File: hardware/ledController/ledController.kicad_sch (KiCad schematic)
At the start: 23 parts, among them IC1 PIC16F1769-I_ML, J1 Conn_01x06, J2 Screw_Terminal_01x02, J3 Screw_Terminal_01x02, J4 Conn_01x06, J5 Conn_01x02_Male

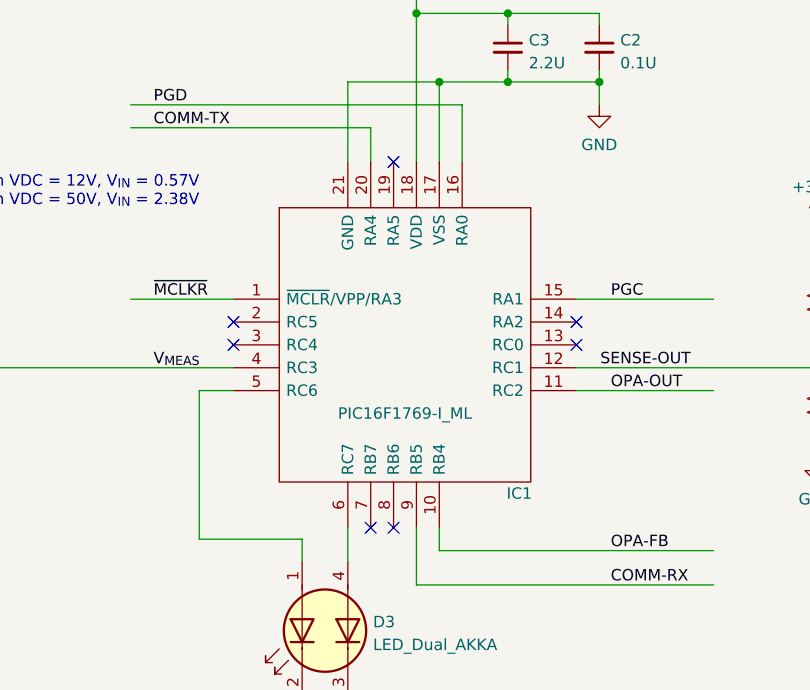
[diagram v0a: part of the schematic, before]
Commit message: Version V1.1
Replaced PIC16F1769 with PIC16LF1709.  They are pin-to-pin
compatible with each other
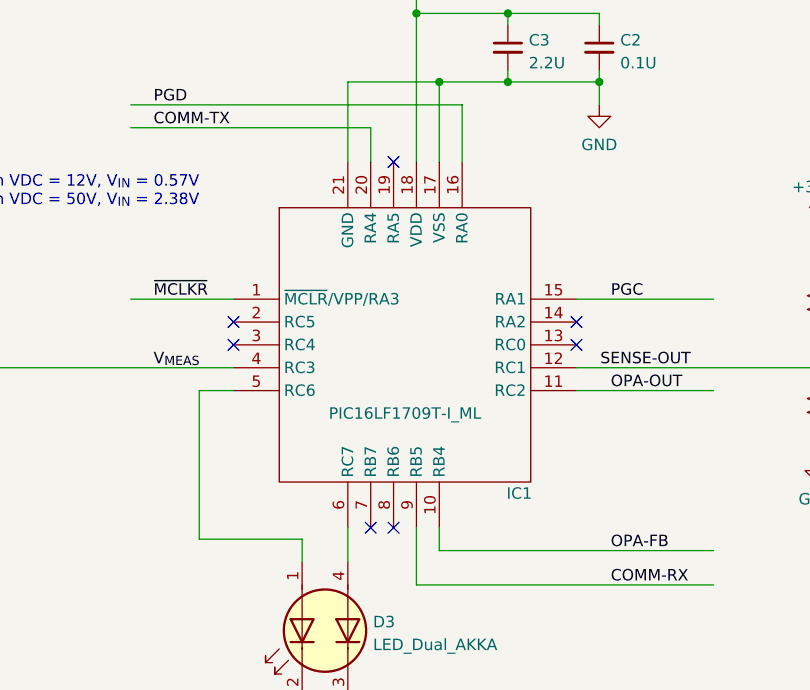
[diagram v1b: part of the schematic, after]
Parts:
- removed IC1: PIC16F1769-I_ML, footprints:QFN50P400X400X100-21N-D, symbol PIC16F1769-I_ML:PIC16F1769-I_ML
- added IC1: PIC16LF1709T-I_ML, Package_DFN_QFN:QFN-20-1EP_4x4mm_P0.5mm_EP2.5x2.5mm, symbol ym_Microcontrollers:PIC16LF1709T-I_ML
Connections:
- net +3.3V: now also IC1.18 (VDD)
- net COMM-RX: now also IC1.9 (RB5)
- net COMM-TX: now also IC1.20 (RA4)
- net GND: now also IC1.17 (VSS), IC1.21 (GND)
- net OPA-FB: now also IC1.10 (RB4)
- net OPA-OUT: now also IC1.11 (RC2)
- net PGC: now also IC1.15 (RA1)
- net PGD: now also IC1.16 (RA0)
- net SENSE-OUT: now also IC1.12 (RC1)
- net V_{MEAS}: now also IC1.4 (RC3)
- net ~{MCLKR}: now also IC1.1 (~{MCLR}/VPP/RA3)
- net at D3.1 (A1): now also IC1.5 (RC6)
- net at D3.4 (A2): now also IC1.6 (RC7)
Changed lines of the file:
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@@
   (title_block
     (title "Lantern")
+    (date "2023-01-09")
+    (rev "V1.1")
   )
   (junction (at 210.82 64.77) (diameter 0) (color 0 0 0 0)
@@
     (pin "2")
   )
-  (symbol (lib_id "PIC16F1769-I_ML:PIC16F1769-I_ML") (at 180.34 88.9 0) (unit 1)
+  (symbol (lib_id "Device:C_Small") (at 220.98 60.96 0) (unit 1)
+    (in_bom yes) (on_board yes) (fields_autoplaced)
+    (property "Reference" "C2" (id 0) (at 223.3041 60.1316 0)
+      (effects (font (size 1.27 1.27)) (justify left))
+    )
+    (property "Value" "0.1U" (id 1) (at 223.3041 62.6685 0)
+      (effects (font (size 1.27 1.27)) (justify left))
+    )
+    (property "Footprint" "Capacitor_SMD:C_0402_1005Metric_Pad0.74x0.62mm_HandSolder" (id 2) (at 220.98 60.96 0)
+      (effects (font (size 1.27 1.27)) hide)
+    )
+    (property "Datasheet" "~" (id 3) (at 220.98 60.96 0)
+      (effects (font (size 1.27 1.27)) hide)
+    )
+    (pin "1")
+    (pin "2")
+  )
+  (symbol (lib_id "Mechanical:MountingHole") (at 172.72 17.78 0) (unit 1)
+    (in_bom yes) (on_board yes) (fields_autoplaced)
+    (property "Reference" "H1" (id 0) (at 175.26 16.9453 0)
+      (effects (font (size 1.27 1.27)) (justify left))
+    )
+    (property "Value" "MountingHole" (id 1) (at 175.26 19.4822 0)
+      (effects (font (size 1.27 1.27)) (justify left))
+    )
+    (property "Footprint" "MountingHole:MountingHole_2.5mm_Pad_TopBottom" (id 2) (at 172.72 17.78 0)
+      (effects (font (size 1.27 1.27)) hide)
+    )
+    (property "Datasheet" "~" (id 3) (at 172.72 17.78 0)
+      (effects (font (size 1.27 1.27)) hide)
+    )
+  )
+  (symbol (lib_id "Device:C_Small") (at 210.82 60.96 0) (unit 1)
+    (in_bom yes) (on_board yes) (fields_autoplaced)
+    (property "Reference" "C3" (id 0) (at 213.1441 60.1316 0)
+      (effects (font (size 1.27 1.27)) (justify left))
+    )
+    (property "Value" "2.2U" (id 1) (at 213.1441 62.6685 0)
+      (effects (font (size 1.27 1.27)) (justify left))
+    )
+    (property "Footprint" "Capacitor_SMD:C_0402_1005Metric_Pad0.74x0.62mm_HandSolder" (id 2) (at 210.82 60.96 0)
+      (effects (font (size 1.27 1.27)) hide)
+    )
+    (property "Datasheet" "~" (id 3) (at 210.82 60.96 0)
+      (effects (font (size 1.27 1.27)) hide)
+    )
+    (pin "1")
+    (pin "2")
+  )
+  (symbol (lib_id "Device:R_Small_US") (at 187.96 140.97 0) (unit 1)
+    (in_bom yes) (on_board yes)
+    (property "Reference" "R11" (id 0) (at 181.61 139.7 0)
+      (effects (font (size 1.27 1.27)) (justify left))
+    )
+    (property "Value" "2.4K" (id 1) (at 181.61 142.24 0)
+      (effects (font (size 1.27 1.27)) (justify left))
+    )
+    (property "Footprint" "Resistor_SMD:R_0603_1608Metric_Pad0.98x0.95mm_HandSolder" (id 2) (at 187.96 140.97 0)
+      (effects (font (size 1.27 1.27)) hide)
+    )
+    (property "Datasheet" "~" (id 3) (at 187.96 140.97 0)
+      (effects (font (size 1.27 1.27)) hide)
+    )
+    (pin "1")
+    (pin "2")
+  )
+  (symbol (lib_id "ym_Microcontrollers:PIC16LF1709T-I_ML") (at 199.39 93.98 0) (unit 1)
     (in_bom yes) (on_board yes)
     (property "Reference" "IC1" (id 0) (at 212.09 110.49 0))
-    (property "Value" "PIC16F1769-I_ML" (id 1) (at 199.39 101.6 0))
-    (property "Footprint" "footprints:QFN50P400X400X100-21N-D" (id 2) (at 214.63 78.74 0)
-      (effects (font (size 1.27 1.27)) (justify left) hide)
-    )
-    (property "Datasheet" "https://componentsearchengine.com/Datasheets/1/PIC16F1769-I_ML.pdf" (id 3) (at 214.63 81.28 0)
-      (effects (font (size 1.27 1.27)) (justify left) hide)
-    )
-    (property "Description" "Microchip Technology PIC16F1769-I/ML, 8bit 8 bit CPU Microcontroller, 32MHz, 14 kB Flash, 20-Pin QFN" (id 4) (at 214.63 83.82 0)
-      (effects (font (size 1.27 1.27)) (justify left) hide)
-    )
-    (property "Height" "1" (id 5) (at 214.63 86.36 0)
-      (effects (font (size 1.27 1.27)) (justify left) hide)
-    )
-    (property "Manufacturer_Name" "Microchip" (id 6) (at 214.63 88.9 0)
-      (effects (font (size 1.27 1.27)) (justify left) hide)
-    )
-    (property "Manufacturer_Part_Number" "PIC16F1769-I/ML" (id 7) (at 214.63 91.44 0)
-      (effects (font (size 1.27 1.27)) (justify left) hide)
-    )
-    (property "Mouser Part Number" "579-PIC16F1769-I/ML" (id 8) (at 214.63 93.98 0)
-      (effects (font (size 1.27 1.27)) (justify left) hide)
-    )
-    (property "Mouser Price/Stock" "https://www.mouser.co.uk/ProductDetail/Microchip-Technology/PIC16F1769-I-ML?qs=4f%252Bx0JRcgJY9K12iAXUX4g%3D%3D" (id 9) (at 214.63 96.52 0)
-      (effects (font (size 1.27 1.27)) (justify left) hide)
-    )
-    (property "Arrow Part Number" "PIC16F1769-I/ML" (id 10) (at 214.63 99.06 0)
-      (effects (font (size 1.27 1.27)) (justify left) hide)
-    )
-    (property "Arrow Price/Stock" "https://www.arrow.com/en/products/pic16f1769-iml/microchip-technology?region=nac" (id 11) (at 214.63 101.6 0)
-      (effects (font (size 1.27 1.27)) (justify left) hide)
-    )
-    (property "Mouser Testing Part Number" "" (id 12) (at 214.63 104.14 0)
-      (effects (font (size 1.27 1.27)) (justify left) hide)
-    )
-    (property "Mouser Testing Price/Stock" "" (id 13) (at 214.63 106.68 0)
-      (effects (font (size 1.27 1.27)) (justify left) hide)
+    (property "Value" "PIC16LF1709T-I_ML" (id 1) (at 199.39 101.6 0))
+    (property "Footprint" "Package_DFN_QFN:QFN-20-1EP_4x4mm_P0.5mm_EP2.5x2.5mm" (id 2) (at 199.39 93.98 0)
+      (effects (font (size 1.27 1.27)) hide)
+    )
+    (property "Datasheet" "https://ww1.microchip.com/downloads/aemDocuments/documents/OTH/ProductDocuments/DataSheets/40001729C.pdf" (id 3) (at 199.39 93.98 0)
+      (effects (font (size 1.27 1.27)) hide)
+    )
+    (property "Description" "Microchip Technology PIC16LF1709T-I_ML, 8-bit CPU Microcontroller, 32MHz, 8KB Flash, 1KB RAM, 20-Pin QFN" (id 4) (at 199.39 93.98 0)
+      (effects (font (size 1.27 1.27)) hide)
     )
     (pin "1")
@@
     (pin "9")
   )
-  (symbol (lib_id "Device:C_Small") (at 220.98 60.96 0) (unit 1)
-    (in_bom yes) (on_board yes) (fields_autoplaced)
-    (property "Reference" "C2" (id 0) (at 223.3041 60.1316 0)
-      (effects (font (size 1.27 1.27)) (justify left))
-    )
-    (property "Value" "0.1U" (id 1) (at 223.3041 62.6685 0)
-      (effects (font (size 1.27 1.27)) (justify left))
-    )
-    (property "Footprint" "Capacitor_SMD:C_0402_1005Metric_Pad0.74x0.62mm_HandSolder" (id 2) (at 220.98 60.96 0)
-      (effects (font (size 1.27 1.27)) hide)
-    )
-    (property "Datasheet" "~" (id 3) (at 220.98 60.96 0)
-      (effects (font (size 1.27 1.27)) hide)
-    )
-    (pin "1")
-    (pin "2")
-  )
-  (symbol (lib_id "Mechanical:MountingHole") (at 172.72 17.78 0) (unit 1)
-    (in_bom yes) (on_board yes) (fields_autoplaced)
-    (property "Reference" "H1" (id 0) (at 175.26 16.9453 0)
-      (effects (font (size 1.27 1.27)) (justify left))
-    )
-    (property "Value" "MountingHole" (id 1) (at 175.26 19.4822 0)
-      (effects (font (size 1.27 1.27)) (justify left))
-    )
-    (property "Footprint" "MountingHole:MountingHole_2.5mm_Pad_TopBottom" (id 2) (at 172.72 17.78 0)
-      (effects (font (size 1.27 1.27)) hide)
-    )
-    (property "Datasheet" "~" (id 3) (at 172.72 17.78 0)
-      (effects (font (size 1.27 1.27)) hide)
-    )
-  )
-  (symbol (lib_id "Device:C_Small") (at 210.82 60.96 0) (unit 1)
-    (in_bom yes) (on_board yes) (fields_autoplaced)
-    (property "Reference" "C3" (id 0) (at 213.1441 60.1316 0)
-      (effects (font (size 1.27 1.27)) (justify left))
-    )
-    (property "Value" "2.2U" (id 1) (at 213.1441 62.6685 0)
-      (effects (font (size 1.27 1.27)) (justify left))
-    )
-    (property "Footprint" "Capacitor_SMD:C_0402_1005Metric_Pad0.74x0.62mm_HandSolder" (id 2) (at 210.82 60.96 0)
-      (effects (font (size 1.27 1.27)) hide)
-    )
-    (property "Datasheet" "~" (id 3) (at 210.82 60.96 0)
-      (effects (font (size 1.27 1.27)) hide)
-    )
-    (pin "1")
-    (pin "2")
-  )
-  (symbol (lib_id "Device:R_Small_US") (at 187.96 140.97 0) (unit 1)
-    (in_bom yes) (on_board yes)
-    (property "Reference" "R11" (id 0) (at 181.61 139.7 0)
-      (effects (font (size 1.27 1.27)) (justify left))
-    )
-    (property "Value" "2.4K" (id 1) (at 181.61 142.24 0)
-      (effects (font (size 1.27 1.27)) (justify left))
-    )
-    (property "Footprint" "Resistor_SMD:R_0603_1608Metric_Pad0.98x0.95mm_HandSolder" (id 2) (at 187.96 140.97 0)
-      (effects (font (size 1.27 1.27)) hide)
-    )
-    (property "Datasheet" "~" (id 3) (at 187.96 140.97 0)
-      (effects (font (size 1.27 1.27)) hide)
-    )
-    (pin "1")
-    (pin "2")
-  )
   (symbol (lib_id "power:GND") (at 220.98 67.31 0) (unit 1)
     (in_bom yes) (on_board yes) (fields_autoplaced)
@@
       (reference "H2") (unit 1) (value "MountingHole") (footprint "MountingHole:MountingHole_2.5mm_Pad_TopBottom")
     )
-    (path "/2d6b1682-0744-43e1-b5bd-1bb30a204cd2"
-      (reference "IC1") (unit 1) (value "PIC16F1769-I_ML") (footprint "footprints:QFN50P400X400X100-21N-D")
+    (path "/44a7638c-2ea4-466c-abcf-8834d0474e02"
+      (reference "IC1") (unit 1) (value "PIC16LF1709T-I_ML") (footprint "Package_DFN_QFN:QFN-20-1EP_4x4mm_P0.5mm_EP2.5x2.5mm")
     )
     (path "/ca01c2f2-1ddc-4048-aeb8-8d47fafcfafe"

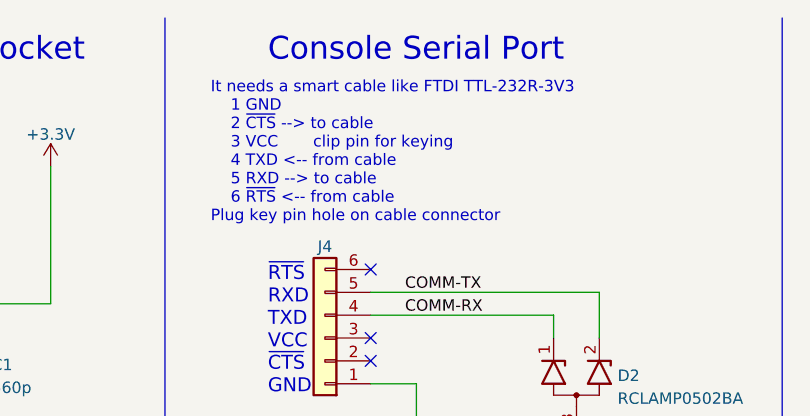
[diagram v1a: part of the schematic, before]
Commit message: Fixed the note for Serial Port connector
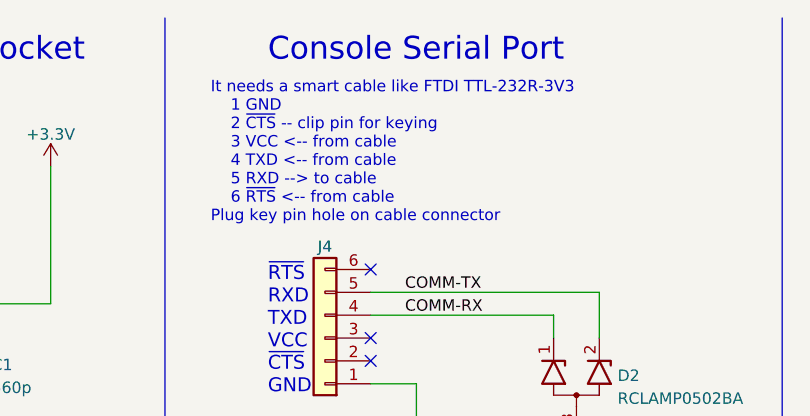
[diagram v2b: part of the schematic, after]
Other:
- note added: "It needs a smart cable like FTDI TTL-232R-3V3 1 GND 2 ~{CTS} -- clip pin for keying 3 VCC <-- from cable 4 TXD <-- from cable 5 RXD --> to cable 6 ~{RTS} <-- from cable Plug key pin hole on cable connector"
- note removed: "It needs a smart cable like FTDI TTL-232R-3V3 1 GND 2 ~{CTS} --> to cable 3 VCC clip pin for keying 4 TXD <-- from cable 5 RXD --> to cable 6 ~{RTS} <-- from cable Plug key pin hole on cable connector"
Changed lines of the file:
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@@
     (effects (font (size 2.54 2.54)) (justify left bottom))
   )
-  (text "It needs a smart cable like FTDI TTL-232R-3V3\n	1 GND\n	2 ~{CTS} --> to cable\n	3 VCC       clip pin for keying\n	4 TXD <-- from cable\n	5 RXD --> to cable\n	6 ~{RTS} <-- from cable\nPlug key pin hole on cable connector"
+  (text "It needs a smart cable like FTDI TTL-232R-3V3\n	1 GND\n	2 ~{CTS} -- clip pin for keying\n	3 VCC <-- from cable\n	4 TXD <-- from cable\n	5 RXD --> to cable\n	6 ~{RTS} <-- from cable\nPlug key pin hole on cable connector"
     (at 72.39 35.56 0)
     (effects (font (size 1.27 1.27)) (justify left bottom))

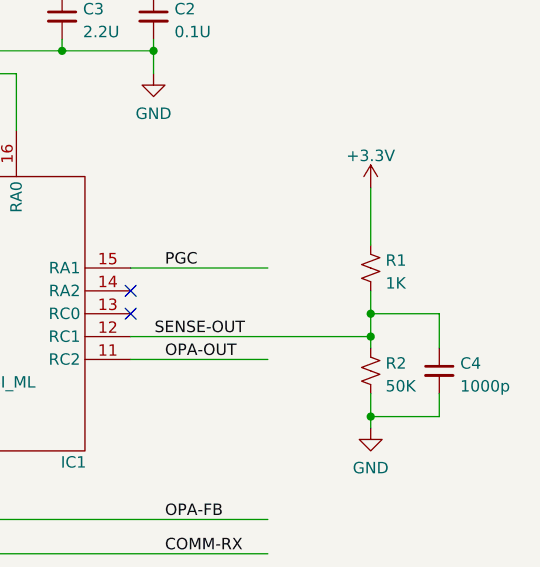
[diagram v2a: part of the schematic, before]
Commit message: Changed R1 from 1K to 15K
Based on the experiments, R1 needs to be close to 15K
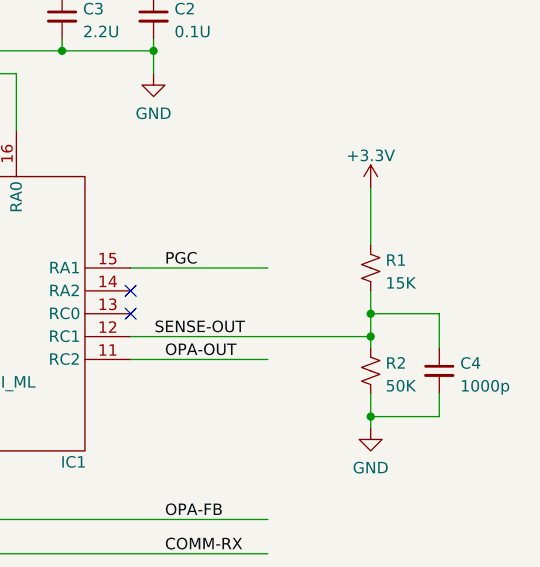
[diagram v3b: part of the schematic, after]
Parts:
- R1: value 1K -> 15K
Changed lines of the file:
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@@
       (effects (font (size 1.27 1.27)) (justify left))
     )
-    (property "Value" "1K" (id 1) (at 246.761 90.6022 0)
+    (property "Value" "15K" (id 1) (at 246.761 90.6022 0)
       (effects (font (size 1.27 1.27)) (justify left))
     )
@@
     )
     (path "/90328c5a-63ab-4227-8ee9-43ae007d29c3"
-      (reference "R1") (unit 1) (value "1K") (footprint "Resistor_SMD:R_0603_1608Metric_Pad0.98x0.95mm_HandSolder")
+      (reference "R1") (unit 1) (value "15K") (footprint "Resistor_SMD:R_0603_1608Metric_Pad0.98x0.95mm_HandSolder")
     )
     (path "/ee662500-be84-4ec7-8cfc-96900a58f9ca"
